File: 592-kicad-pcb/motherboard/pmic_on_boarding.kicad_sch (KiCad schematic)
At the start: 0 parts

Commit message: working through switching
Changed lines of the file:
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@@
+		)
+	)
+	(wire
+		(pts
+			(xy 33.02 48.26) (xy 35.56 48.26)
+		)
+		(stroke
+			(width 0)
+			(type default)
+		)
+	)
+	(hierarchical_label "GND"
+		(shape bidirectional)
+		(at 35.56 48.26 0)
+		(effects
+			(font
+				(size 1.27 1.27)
+			)
+			(justify left)
 		)
 	)

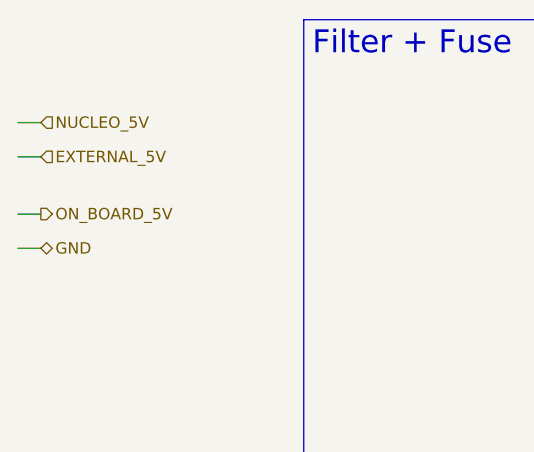
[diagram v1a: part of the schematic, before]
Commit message: pmic switching schem done
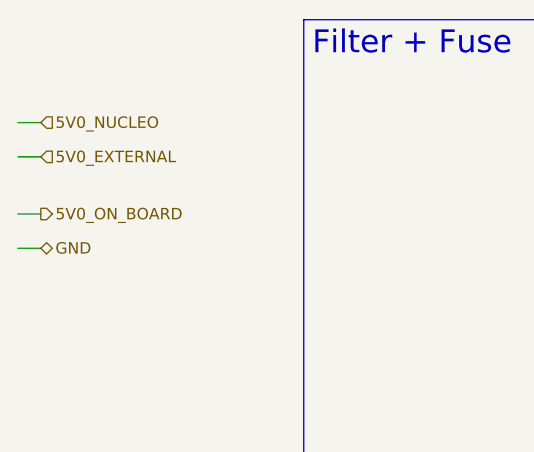
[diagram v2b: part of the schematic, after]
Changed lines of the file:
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@@
 		)
 	)
-	(hierarchical_label "ON_BOARD_5V"
+	(hierarchical_label "5V0_ON_BOARD"
 		(shape output)
 		(at 35.56 44.45 0)
@@
 		)
 	)
-	(hierarchical_label "NUCLEO_5V"
+	(hierarchical_label "5V0_NUCLEO"
 		(shape input)
 		(at 35.56 34.29 0)
@@
 		)
 	)
-	(hierarchical_label "EXTERNAL_5V"
+	(hierarchical_label "5V0_EXTERNAL"
 		(shape input)
 		(at 35.56 38.1 0)

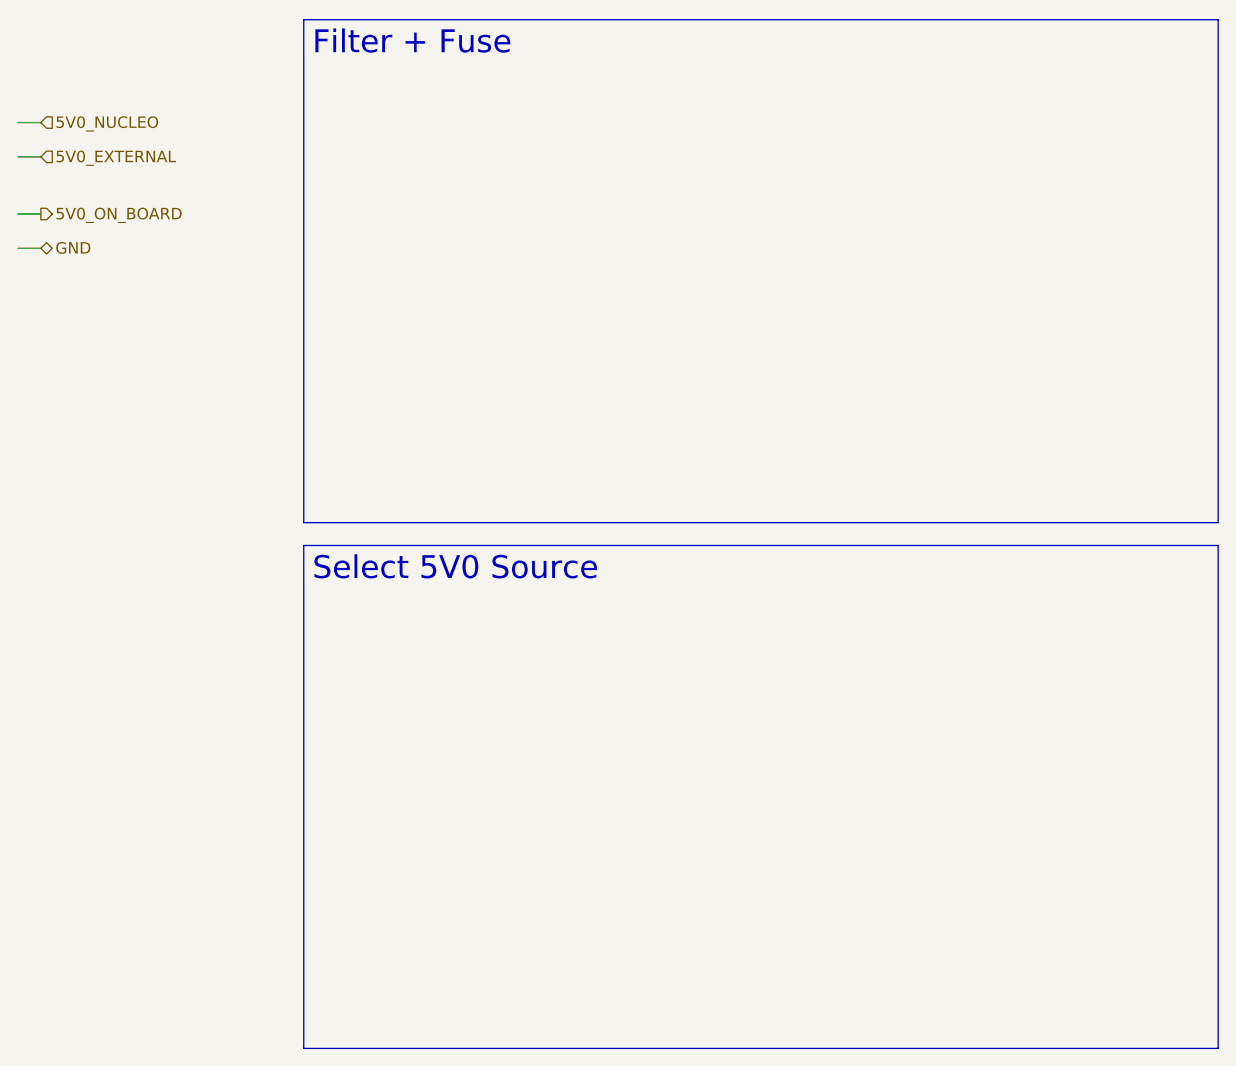
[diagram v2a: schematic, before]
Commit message: fuses, ferrite bead, 5V0 selection connector
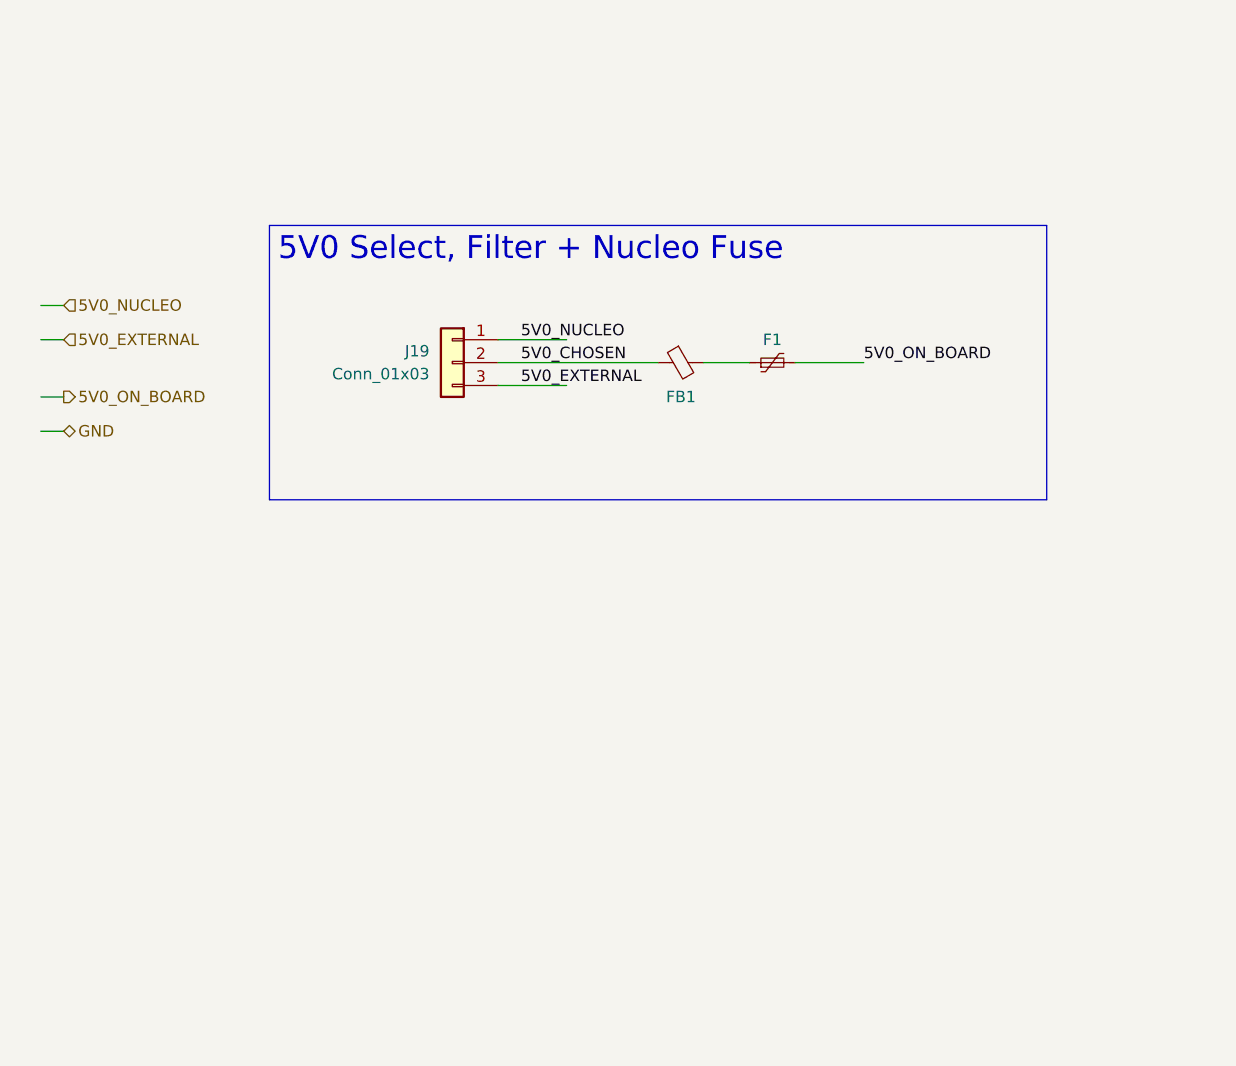
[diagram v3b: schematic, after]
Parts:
- added F1: (no value), 0805, symbol Device:Polyfuse_Small
- added FB1: (no value), 0402, symbol Device:FerriteBead_Small
- added J19: Conn_01x03, symbol Connector_Generic:Conn_01x03
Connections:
- net 5V0_EXTERNAL: now also J19.3 (Pin_3)
- net 5V0_NUCLEO: now also J19.1 (Pin_1)
- net 5V0_ON_BOARD: now also F1.2
- new net: F1.1, FB1.2
- new net 5V0_CHOSEN: FB1.1, J19.2 (Pin_2)

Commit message: supply connectors, solder bridges
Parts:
- F1, FB1: value (none) -> ~
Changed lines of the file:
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@@
 			)
 		)
-		(property "Value" ""
+		(property "Value" "~"
 			(at 116.84 57.658 90)
 			(effects
@@
 			)
 		)
-		(property "Value" ""
+		(property "Value" "~"
 			(at 106.6419 64.77 90)
 			(effects

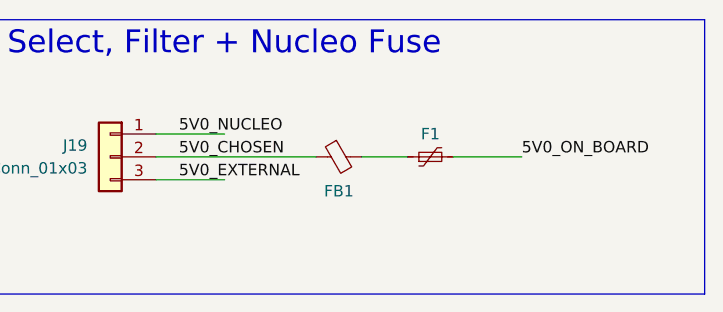
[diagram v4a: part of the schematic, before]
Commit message: fuse, fb info in values
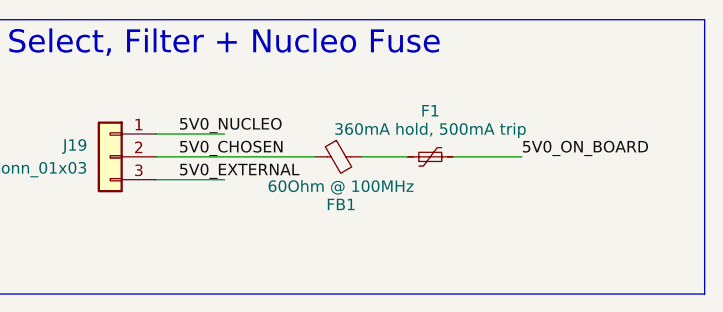
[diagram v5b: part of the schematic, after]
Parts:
- F1: value ~ -> 360mA hold, 500mA trip
- FB1: value ~ -> 60Ohm @ 100MHz
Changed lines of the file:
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@@
 		(dnp no)
 		(property "Reference" "F1"
-			(at 116.84 58.42 90)
+			(at 116.84 55.88 90)
 			(effects
 				(font
@@
 			)
 		)
-		(property "Value" "~"
-			(at 116.84 57.658 90)
+		(property "Value" "360mA hold, 500mA trip"
+			(at 116.84 57.912 90)
 			(effects
 				(font
@@
 		(dnp no)
 		(property "Reference" "FB1"
-			(at 106.68 64.77 90)
+			(at 106.934 66.294 90)
 			(effects
 				(font
@@
 			)
 		)
-		(property "Value" "~"
-			(at 106.6419 64.77 90)
+		(property "Value" "60Ohm @ 100MHz"
+			(at 106.8959 64.262 90)
 			(effects
 				(font

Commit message: john's notes
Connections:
- no-connect marks 0 -> 5
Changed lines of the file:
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@@
 		)
+	)
+	(no_connect
+		(at 127 60.96)
+	)
+	(no_connect
+		(at 35.56 58.42)
+	)
+	(no_connect
+		(at 35.56 68.58)
+	)
+	(no_connect
+		(at 35.56 53.34)
+	)
+	(no_connect
+		(at 35.56 63.5)
 	)
 	(wire
@@
 	(wire
 		(pts
-			(xy 35.56 64.77) (xy 38.1 64.77)
+			(xy 35.56 63.5) (xy 38.1 63.5)
 		)
 		(stroke
@@
 	(wire
 		(pts
-			(xy 35.56 54.61) (xy 38.1 54.61)
+			(xy 35.56 53.34) (xy 38.1 53.34)
 		)
 		(stroke
@@
 	(hierarchical_label "5V0_ON_BOARD"
 		(shape output)
-		(at 38.1 64.77 0)
+		(at 38.1 63.5 0)
 		(effects
 			(font
@@
 	(hierarchical_label "5V0_NUCLEO"
 		(shape input)
-		(at 38.1 54.61 0)
+		(at 38.1 53.34 0)
 		(effects
 			(font

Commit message: updates to routing
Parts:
- renumbered J19 to J27
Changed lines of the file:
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@@
 		(on_board yes)
 		(dnp no)
-		(property "Reference" "J19"
+		(property "Reference" "J27"
 			(at 78.74 59.6899 0)
 			(effects
@@
 			(project ""
 				(path "/5b0c97ac-fa03-4db8-b41b-0eee32b6f55d/f049e4ad-bebe-4338-850a-2727de737ae9/dbe4469e-0fdf-4a67-ba41-36d27b688d04"
-					(reference "J19")
+					(reference "J27")
 					(unit 1)
 				)
